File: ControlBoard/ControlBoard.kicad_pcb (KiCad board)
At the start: 2 copper layers, 127 x 27.9 mm, 11 parts

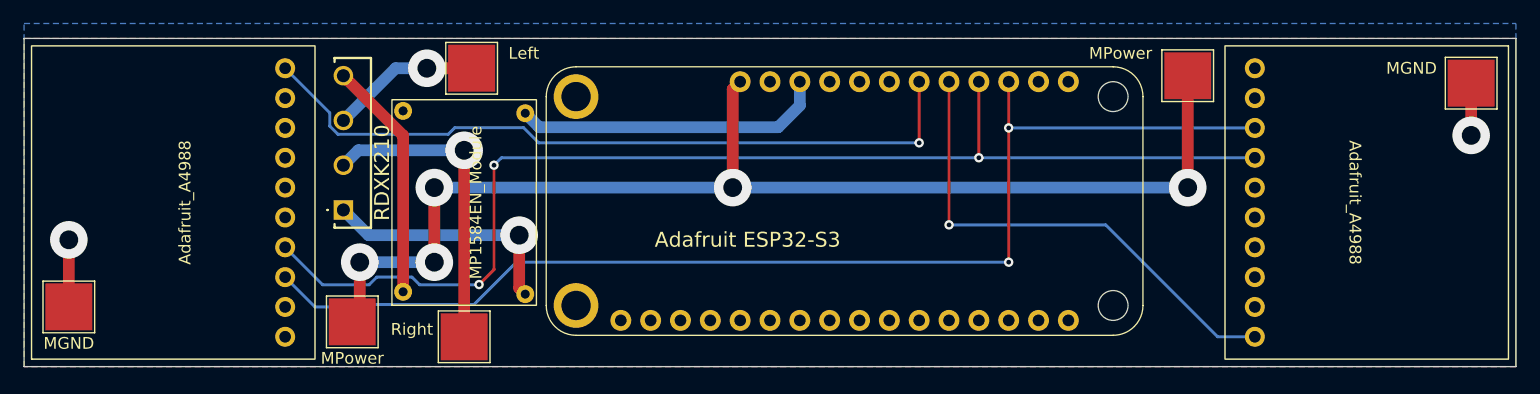
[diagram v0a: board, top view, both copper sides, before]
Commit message: Add Sleep. Start on the firmware.
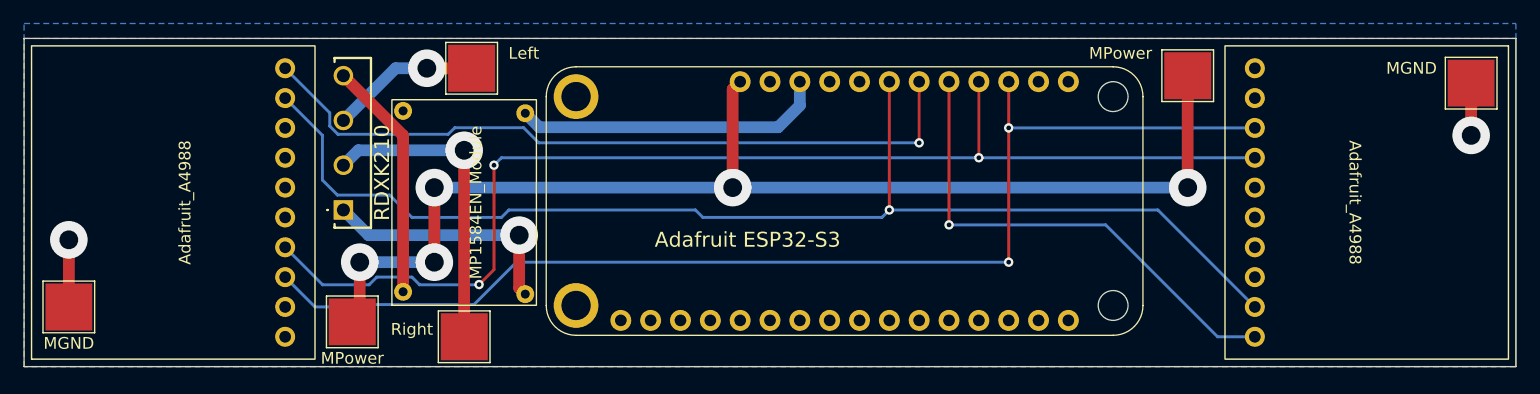
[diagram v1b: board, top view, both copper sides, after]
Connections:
- MS101 pad 9: unconnected-(MS101-Pad9) -> /CommonSLP
- MS102 pad 23: unconnected-(MS102-Pad23) -> /CommonSLP
- MS103 pad 9: unconnected-(MS103-Pad9) -> /CommonSLP
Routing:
- net /CommonSLP: track 0.00 -> 104.1 mm, vias 0 -> 1
